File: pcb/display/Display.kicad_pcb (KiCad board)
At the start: 2 copper layers, 100 x 75 mm, 209 parts, among them J1 XH 2P, J101 RJ45, J102 Screw Terminal 3.5mm, J103 01x08_Pin, J105 U.FL, J201 Term 3.5mm, J202 Term 3.5mm, J401 XH 2P, J402 XH 2P, J403 XH 2P, J404 XH 2P, J405 XH 2P, J406 XH 2P, J407 XH 2P, J501 XH 2P, J502 XH 2P, J503 XH 2P, J504 XH 2P, J505 XH 2P, J506 XH 2P, J507 XH 2P, P101 USB_C_Plug_USB2.0, Q101 2N7002, Q201 DOZ35N06, Q202 DOZ35N06, Q401 DOZ35N06, Q402 DOZ35N06, Q403 DOZ35N06, Q404 DOZ35N06, Q405 DOZ35N06, Q406 DOZ35N06, Q407 DOZ35N06, Q501 DOZ35N06, Q502 DOZ35N06, Q503 DOZ35N06, Q504 DOZ35N06, Q505 DOZ35N06, Q506 DOZ35N06, Q507 DOZ35N06, Q601 DOZ35N06, Q602 DOZ35N06, SW101 SW_4x3mm, SW102 SW_4x3mm, SW103 SW_4x3mm, SW104 SW_4x3mm, U101 TMP1075DSGR, U102 ESP32-S3FN8, U201 PCA9685BS, U301 SP3485EN-L/TR, U302 E220-400M22S, U601 SIC438BED-T1-GE3, U602 TPS259474ARPWR, U603 TPS54202DDC, U604 TPS54202DDC, U605 LM74700, U606 LM74700, Y101 3225 40MHz 10ppm

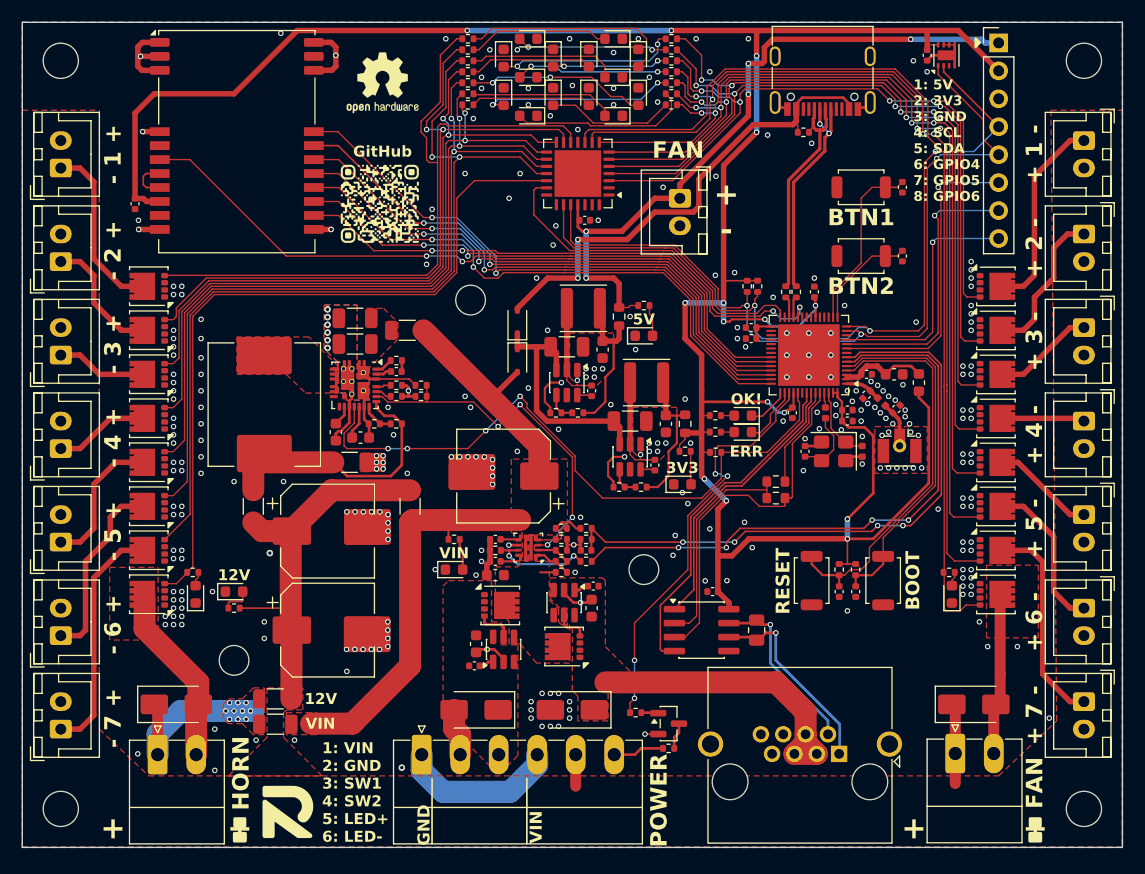
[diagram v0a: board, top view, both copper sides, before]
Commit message: Adjusted footprint of mosfets for 0.15mm solder mask spacing
New Gerber files
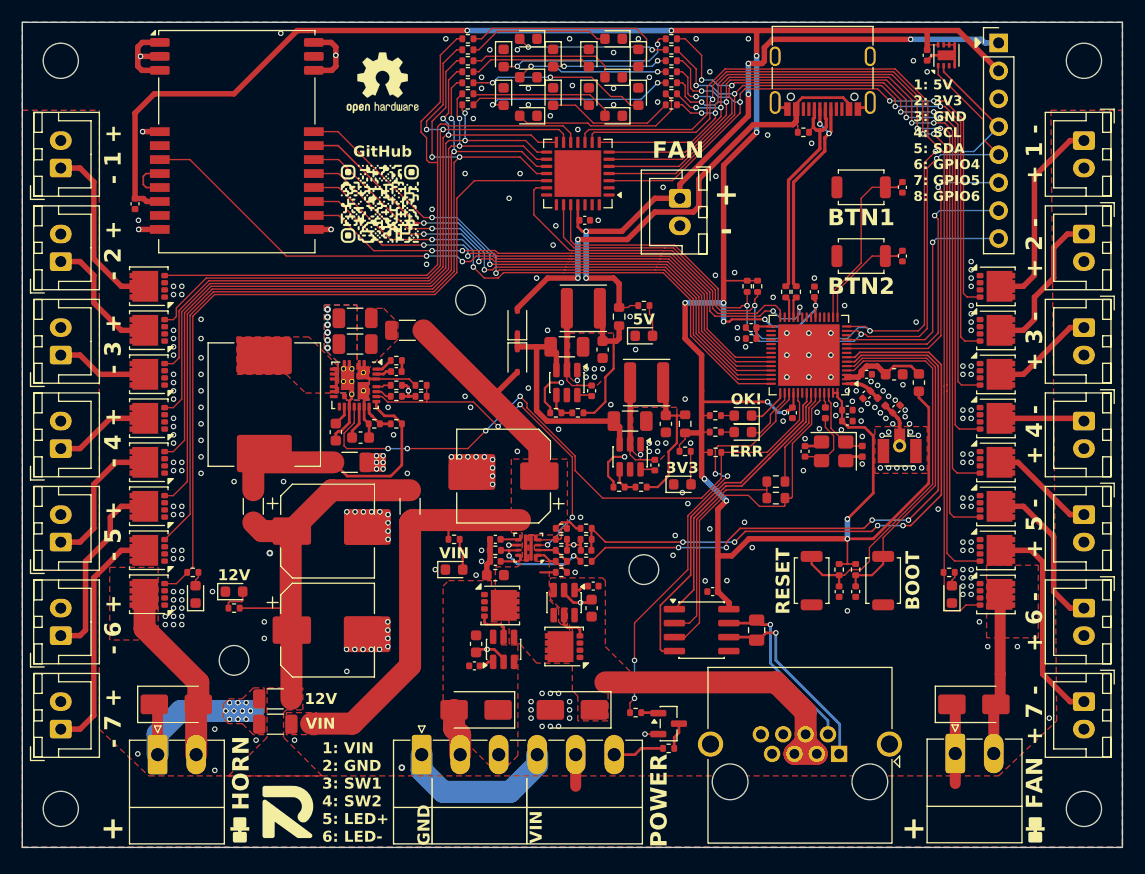
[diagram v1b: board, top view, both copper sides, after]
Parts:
- Q201, Q202, Q401, Q402, Q403, Q404, Q405, Q406, Q407, Q501, Q502, Q503, Q504, Q505, Q506, Q507, Q601, Q602: footprint Package_SON:VSON-8_3.3x3.3mm_P0.65mm_NexFET -> RVNSPRK_Packages:VSON-8_3.3x3.3mm_P0.65mm_Custom

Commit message: Changed some Part# for production based on feedback an availability
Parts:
- C607, C608, C612: value 150u -> 220u
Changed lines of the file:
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@@
 			)
 		)
+		(property "LCSC Part #" "C6332201"
+			(at 0 0 0)
+			(unlocked yes)
+			(layer "F.Fab")
+			(hide yes)
+			(effects
+				(font
+					(size 1 1)
+					(thickness 0.15)
+				)
+			)
+		)
 		(property ki_fp_filters "Connector*:*_1x??_*")
 		(sheetname "/")
@@
 			)
 		)
-		(property "Value" "150u"
+		(property "Value" "220u"
 			(at 0 5.2 0)
 			(layer "F.Fab")
@@
 			)
 		)
-		(property "LCSC Part #" "C5373402"
+		(property "LCSC Part #" "C5246542"
 			(at 0 0 0)
 			(unlocked yes)
@@
 			)
 		)
-		(property "Value" "150u"
+		(property "Value" "220u"
 			(at 0 5.2 0)
 			(layer "F.Fab")
@@
 			)
 		)
-		(property "LCSC Part #" "C5373402"
+		(property "LCSC Part #" "C5246542"
 			(at 0 0 0)
 			(unlocked yes)
@@
 			)
 		)
-		(property "LCSC Part #" "C307331"
+		(property "LCSC Part #" "C76948"
 			(at 0 0 90)
 			(unlocked yes)
@@
 		(sheetname "/")
 		(sheetfile "Display.kicad_sch")
-		(attr exclude_from_pos_files allow_missing_courtyard)
+		(attr exclude_from_pos_files exclude_from_bom allow_missing_courtyard)
 		(fp_poly
 			(pts
@@
 			)
 		)
-		(property "LCSC Part #" "C307331"
+		(property "LCSC Part #" "C76948"
 			(at 0 0 270)
 			(unlocked yes)
@@
 			)
 		)
-		(property "Value" "150u"
+		(property "Value" "220u"
 			(at 0 5.2 0)
 			(layer "F.Fab")
@@
 			)
 		)
-		(property "LCSC Part #" "C5373402"
+		(property "LCSC Part #" "C5246542"
 			(at 0 0 180)
 			(unlocked yes)
@@
 		(sheetname "/")
 		(sheetfile "Display.kicad_sch")
-		(attr exclude_from_pos_files allow_missing_courtyard)
+		(attr exclude_from_pos_files exclude_from_bom allow_missing_courtyard)
 		(fp_poly
 			(pts
